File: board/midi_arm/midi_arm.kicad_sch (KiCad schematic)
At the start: 25 parts, among them J1 Conn_01x02_Pin, J2 Conn_01x02_Pin, J3 Conn_01x10_Pin, J4 RJ45, J5 Conn_01x03_Pin, J6 Conn_01x03_Pin, J7 Conn_01x03_Pin, U6 6DOF_6050

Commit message: BABOI 2.0 Board
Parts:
- removed C1, C2, C3: 100nF, Capacitor_SMD:C_01005_0402Metric, symbol Device:C
- removed J1, J2: Conn_01x02_Pin, Connector_PinHeader_2.54mm:PinHeader_1x02_P2.54mm_Vertical, symbol Connector:Conn_01x02_Pin
- removed J3: Conn_01x10_Pin, Connector_PinHeader_2.54mm:PinHeader_1x10_P2.54mm_Vertical, symbol Connector:Conn_01x10_Pin
- removed J4: RJ45, Connector_RJ:RJ45_Ninigi_GE, symbol Connector:RJ45
- removed J5, J6, J7: Conn_01x03_Pin, Connector_PinHeader_2.54mm:PinHeader_1x03_P2.54mm_Vertical, symbol Connector:Conn_01x03_Pin
- removed U1: ~, midi_arm:Wemos_S3_Mini_Outer_Pins, symbol midi_arm:Wemos_S3_Mini_Outer_Pins
- removed U2, U3, U4, U7: ~, midi_arm:TOUCH_BAR, symbol midi_arm:CAP_BUT_STRIP
- added H7, H8: MountingHole, MountingHole:MountingHole_2.2mm_M2, symbol Mechanical:MountingHole
- added J1: Conn_01x06_Pin, GPB_Footprints:JST_1x6_2.54, symbol Connector:Conn_01x06_Pin
- added J10, J5, J6, J7, J9: Conn_01x01_Pin, Connector_PinHeader_1.27mm:PinHeader_1x01_P1.27mm_Vertical, symbol Connector:Conn_01x01_Pin
- added J2: Conn_01x03_Pin, midi_arm:LED_conn, symbol Connector:Conn_01x03_Pin
- added J3: Conn_01x08_Pin, Connector_PinHeader_2.54mm:PinHeader_1x08_P2.54mm_Vertical, symbol Connector:Conn_01x08_Pin
- added J4: Conn_01x05_Pin, GPB_Footprints:JST_1x5_2.54_cablepad, symbol Connector:Conn_01x05_Pin
- added J8: Conn_01x06_Pin, GPB_Footprints:JST_1x6_2.54_cablepad, symbol Connector:Conn_01x06_Pin
- added R1, R11, R12, R13, R14, R16, R17, R18, R19, R2, R3, R4, R6, R7, R8, R9: 2.4k, Resistor_SMD:R_0805_2012Metric_Pad1.20x1.40mm_HandSolder, symbol Device:R
- added R10, R15, R20, R5: 24k, Resistor_SMD:R_0805_2012Metric_Pad1.20x1.40mm_HandSolder, symbol Device:R
- added RV1, RV2, RV3, RV4: R_Potentiometer_Small, midi_arm:pot_9.5x9.5, symbol Device:R_Potentiometer_Small
- added SW1, SW2, SW3, SW4: SW_MEC_5E, GPB_Footprints:switch_Touchpad, symbol Switch:SW_MEC_5E
- added U1: ~, GPB_Footprints:ESP32_S2_Wemos_Mini, symbol GPB_Parts:ESP32S2_Mini_Mod
- added U7, U9: ~, Package_DIP:DIP-8_W7.62mm, symbol midi_arm:MCP6002
- added U8: ~, midi_arm:ADS1115_mod, symbol midi_arm:ADS1115_mod
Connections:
- net GND1: now also J1.1 (Pin_1), J2.1 (Pin_1), J3.1 (Pin_1), SW1.3 (K), SW2.3 (K), SW3.3 (K), SW4.3 (K), U1.10A (GND), U1.10B (GND)
- net VBUS: now also J2.3 (Pin_3), J3.7 (Pin_7), U1.9A (VBUS)
- net at D2.2 (DOUT): now also J2.2 (Pin_2)
- net VCC_3V3: now reaches U5.1 (VCC)
- net VCC_3V3: now also J1.6 (Pin_6), J3.8 (Pin_8), U1.8A (VCC_3V3)
- net GLOVE_VCC: now reaches U6.1 (VCC)
- net GLOVE_VCC: now also J8.6 (Pin_6), R1.1, R11.1, R12.1, R16.1, R17.1, R3.1, R6.1, R7.1, U7.8 (VDD), U8.1 (Vcc), U9.8 (VDD)
- net GND2: now reaches U6.2 (GND)
- net GND2: now also J4.5 (Pin_5), J5.1 (Pin_1), J8.1 (Pin_1), R13.2, R18.2, R2.2, R8.2, U7.4 (GND), U8.2 (GND), U9.4 (GND)
- net GLOVE_SCL: now reaches U6.3 (SCL)
- net GLOVE_SCL: now also J8.3 (Pin_3), U8.3 (SCL)
- net GLOVE_SDA: now reaches U6.4 (SDA)
- net GLOVE_SDA: now also J8.4 (Pin_4), U8.4 (SDA)
- net GLOVE_ACC_INT: now reaches U6.8 (INT)
- net GLOVE_ACC_INT: now also J8.2 (Pin_2)
- net at D1.4 (DIN): now also U1.16A (GPIO_39)
- net SCL: now reaches U5.3 (SCL)
- net SCL: now also U1.3A (GPIO_5)
- net SDA: now reaches U5.4 (SDA)
- net SDA: now also U1.4A (GPIO_7)
- net at U5.8 (INT): now also U1.12A (GPIO_18)
- new net: SW1.2, U1.5A (GPIO_9)
- new net: R16.2, R18.1, R19.1
- new net: R19.2, R20.1, U9.6 (VinB-)
- new net: J10.1 (Pin_1), R17.2, RV1.2, U9.5 (VinB+)
- new net: R10.1, R9.2, U7.6 (VinB-)
- new net: R10.2, U7.7 (VoutB), U8.9 (A2)
- new net: J4.4 (Pin_4), RV4.1
- new net: J6.1 (Pin_1), R3.2, RV4.2, U7.3 (VinA+)
- new net: J4.1 (Pin_1), RV1.1
- new net: J4.2 (Pin_2), RV2.1
- new net: J4.3 (Pin_3), RV3.1
- new net: J7.1 (Pin_1), R7.2, RV3.2, U7.5 (VinB+)
- new net: R4.2, R5.1, U7.2 (VinA-)
- new net: R5.2, U7.1 (VoutA), U8.10 (A3)
- new net: R11.2, R13.1, R14.1
- new net: R14.2, R15.1, U9.2 (VinA-)
- new net: R20.2, U8.7 (A0), U9.7 (VoutB)
- new net: SW4.2, U1.2B (GPIO_2)
- new net: J9.1 (Pin_1), R12.2, RV2.2, U9.3 (VinA+)
- new net: R1.2, R2.1, R4.1
- new net: R6.2, R8.1, R9.1
- new net: SW2.2, U1.2A (GPIO_3)
- new net: SW3.2, U1.6B (GPIO_10)
- new net: R15.2, U8.8 (A1), U9.1 (VoutA)
- new net ALERT: J1.5 (Pin_5), U1.15A (GPIO_37)
- new net EXT_D0: J3.2 (Pin_2), U1.3B (GPIO_4)
- new net EXT_D1: J3.3 (Pin_3), U1.4B (GPIO_6)
- new net EXT_D2: J3.4 (Pin_4), U1.5B (GPIO_8)
- new net EXT_D3: J3.5 (Pin_5), U1.1B (GPIO_1)
- new net EXT_INT: J3.6 (Pin_6), U1.11A (GPIO_16)
- new net EXT_SCL: J1.3 (Pin_3), U1.12B (GPIO_21)
- new net EXT_SDA: J1.4 (Pin_4), U1.16B (GPIO_40)
- new net GLOVE_ADC_ALERT: J8.5 (Pin_5), U8.6 (ALERT)
- new net INT: J1.2 (Pin_2), U1.14A (GPIO_35)
- no-connect marks 11 -> 32
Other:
- note added: "A"
- note added: "B"
- note added: "C"
- note added: "CTRL"
- note added: "Design Target for Tension Strips is 1.4 - 1.6 kOhm +/- 500 Ohm"
- note added: "ESP32-S2"
- note added: "Extension Port"
- note added: "Glove Board"
- note added: "Glove Board Conn"
- note added: "Glove Connector"
- note added: "LED"
- note added: "Tension Strips"
- note removed: "3_3V"
- note removed: "TOUCH1"
- note removed: "TOUCH2"
- note removed: "TOUCH3"
- note removed: "VBUS"
- title: (none) -> BABOI
- moved on the sheet: D1, D2, H1, H2, H3, H4, H5, H6, U5, U6

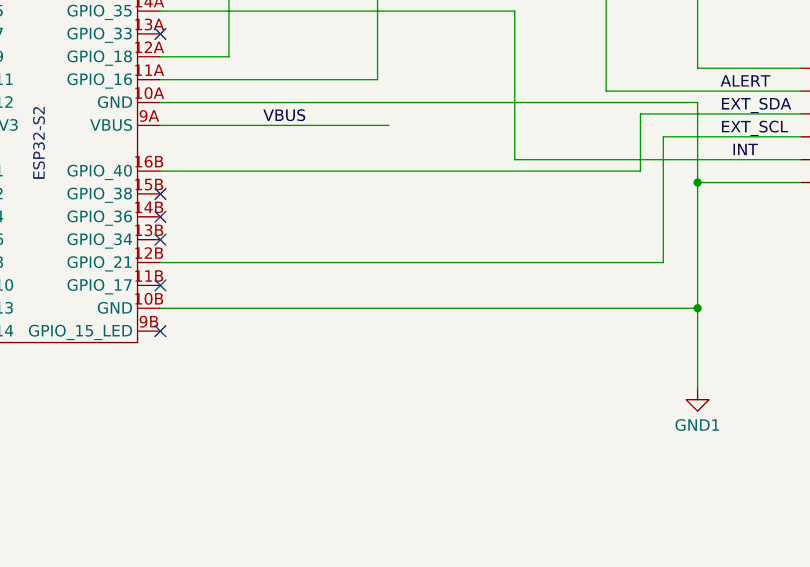
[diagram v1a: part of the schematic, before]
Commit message: Add support for touchpads vs buttons
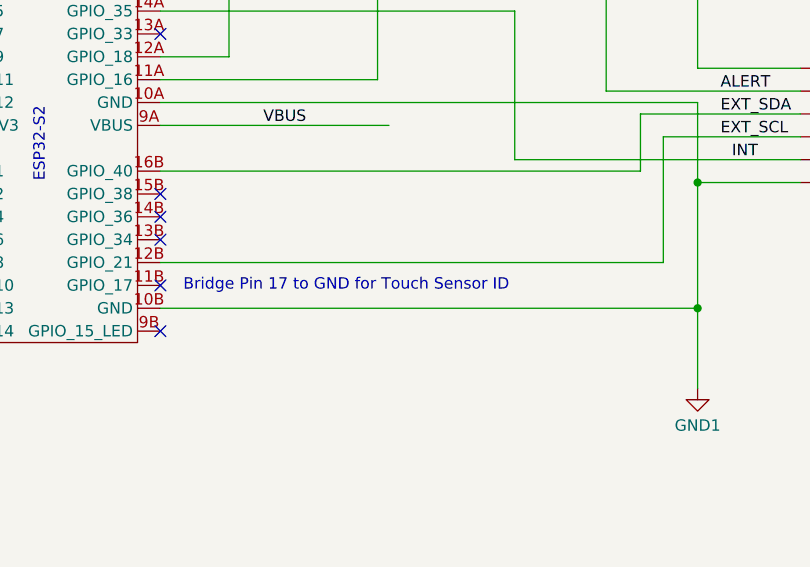
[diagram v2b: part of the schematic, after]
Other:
- note added: "Bridge Pin 17 to GND for Touch Sensor ID"
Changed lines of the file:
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@@
+    (effects (font (size 1.27 1.27)) (justify left bottom))
+  )
+  (text "Bridge Pin 17 to GND for Touch Sensor ID" (at 194.31 129.032 0)
     (effects (font (size 1.27 1.27)) (justify left bottom))
   )

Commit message: updates
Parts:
- R12, R17, R3, R7: value 2.4k -> 5.1k
- R13, R14, R18, R19, R2, R4, R8, R9: value 2.4k -> 3.3k
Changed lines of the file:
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@@
       (effects (font (size 1.27 1.27)))
     )
-    (property "Value" "2.4k" (at 77.47 29.0139 90)
+    (property "Value" "3.3k" (at 77.47 29.0139 90)
       (effects (font (size 1.27 1.27)))
     )
@@
       (effects (font (size 1.27 1.27)))
     )
-    (property "Value" "2.4k" (at 34.29 34.0939 90)
+    (property "Value" "5.1k" (at 34.29 34.0939 90)
       (effects (font (size 1.27 1.27)))
     )
@@
       (effects (font (size 1.27 1.27)))
     )
-    (property "Value" "2.4k" (at 77.47 46.7939 90)
+    (property "Value" "3.3k" (at 77.47 46.7939 90)
       (effects (font (size 1.27 1.27)))
     )
@@
       (effects (font (size 1.27 1.27)))
     )
-    (property "Value" "2.4k" (at 77.47 82.3539 90)
+    (property "Value" "3.3k" (at 77.47 82.3539 90)
       (effects (font (size 1.27 1.27)))
     )
@@
       (effects (font (size 1.27 1.27)))
     )
-    (property "Value" "2.4k" (at 34.29 87.4339 90)
+    (property "Value" "5.1k" (at 34.29 87.4339 90)
       (effects (font (size 1.27 1.27)))
     )
@@
       (effects (font (size 1.27 1.27)))
     )
-    (property "Value" "2.4k" (at 34.29 51.8739 90)
+    (property "Value" "5.1k" (at 34.29 51.8739 90)
       (effects (font (size 1.27 1.27)))
     )
@@
       (effects (font (size 1.27 1.27)))
     )
-    (property "Value" "2.4k" (at 77.47 64.5739 90)
+    (property "Value" "3.3k" (at 77.47 64.5739 90)
       (effects (font (size 1.27 1.27)))
     )
@@
       (effects (font (size 1.27 1.27)))
     )
-    (property "Value" "2.4k" (at 34.29 69.6539 90)
+    (property "Value" "5.1k" (at 34.29 69.6539 90)
       (effects (font (size 1.27 1.27)))
     )
@@
       (effects (font (size 1.27 1.27)))
     )
-    (property "Value" "2.4k" (at 46.99 25.2039 90)
+    (property "Value" "3.3k" (at 46.99 25.2039 90)
       (effects (font (size 1.27 1.27)))
     )
@@
       (effects (font (size 1.27 1.27)))
     )
-    (property "Value" "2.4k" (at 46.99 60.7639 90)
+    (property "Value" "3.3k" (at 46.99 60.7639 90)
       (effects (font (size 1.27 1.27)))
     )
@@
       (effects (font (size 1.27 1.27)))
     )
-    (property "Value" "2.4k" (at 46.99 78.5439 90)
+    (property "Value" "3.3k" (at 46.99 78.5439 90)
       (effects (font (size 1.27 1.27)))
     )
@@
       (effects (font (size 1.27 1.27)))
     )
-    (property "Value" "2.4k" (at 46.99 42.9839 90)
-      (effects (font (size 1.27 1.27)))
-    )
+    (property "Value" "3.3k" (at 46.99 42.9839 90)
+      (effects (font (size 1.27 1.27)))
+    )

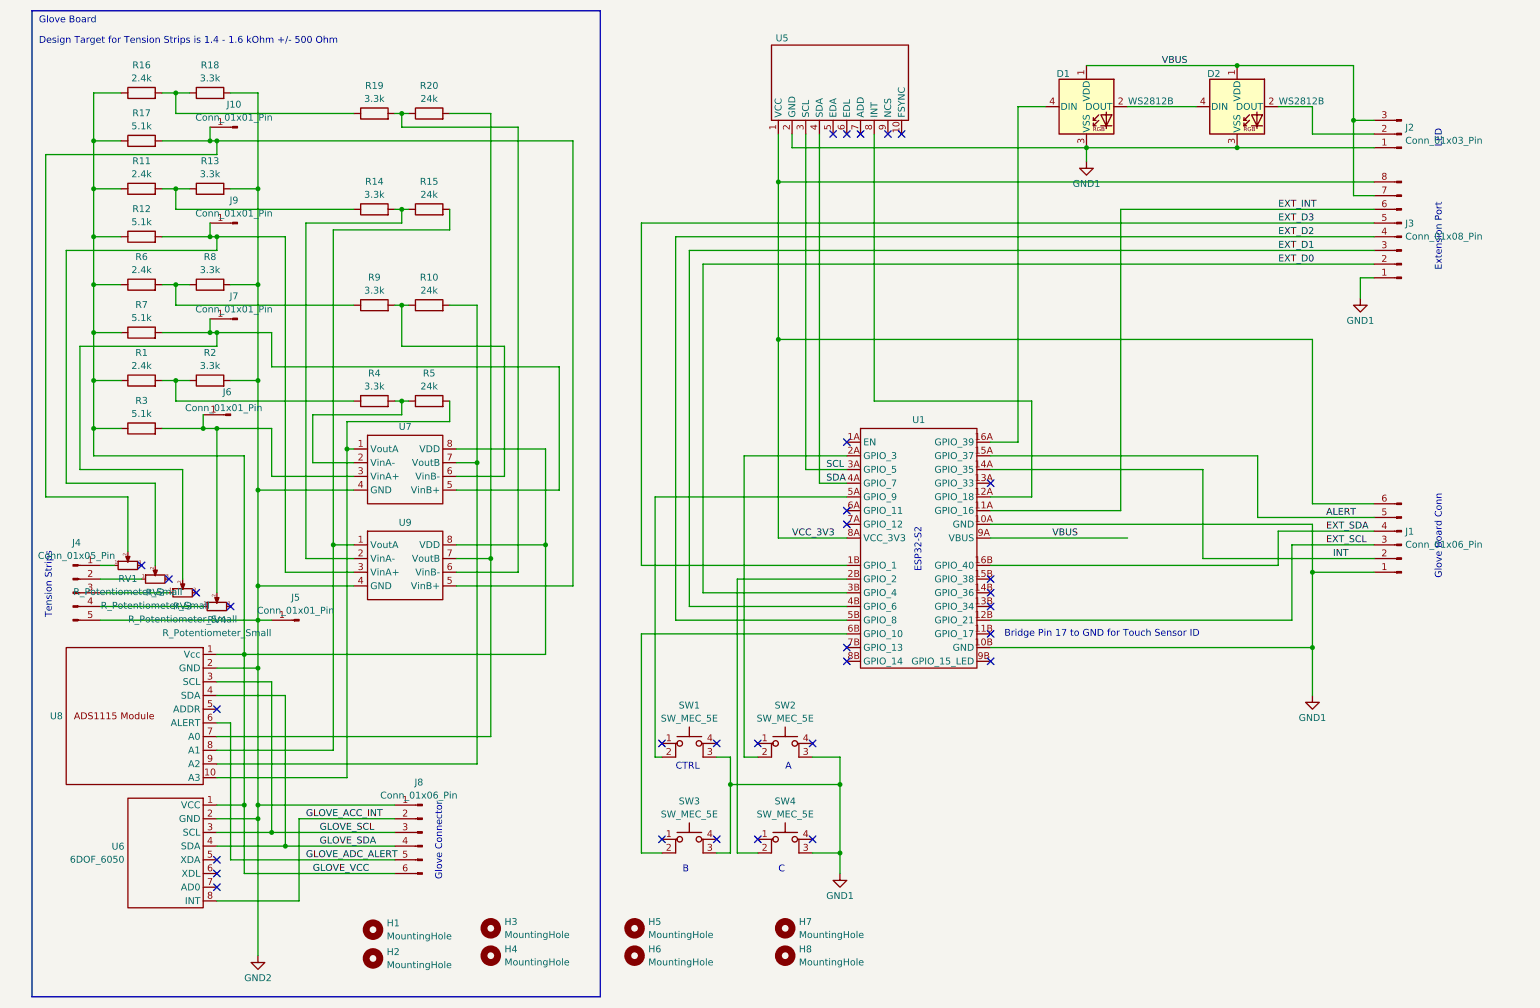
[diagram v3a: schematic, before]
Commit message: HW Version 3 Support
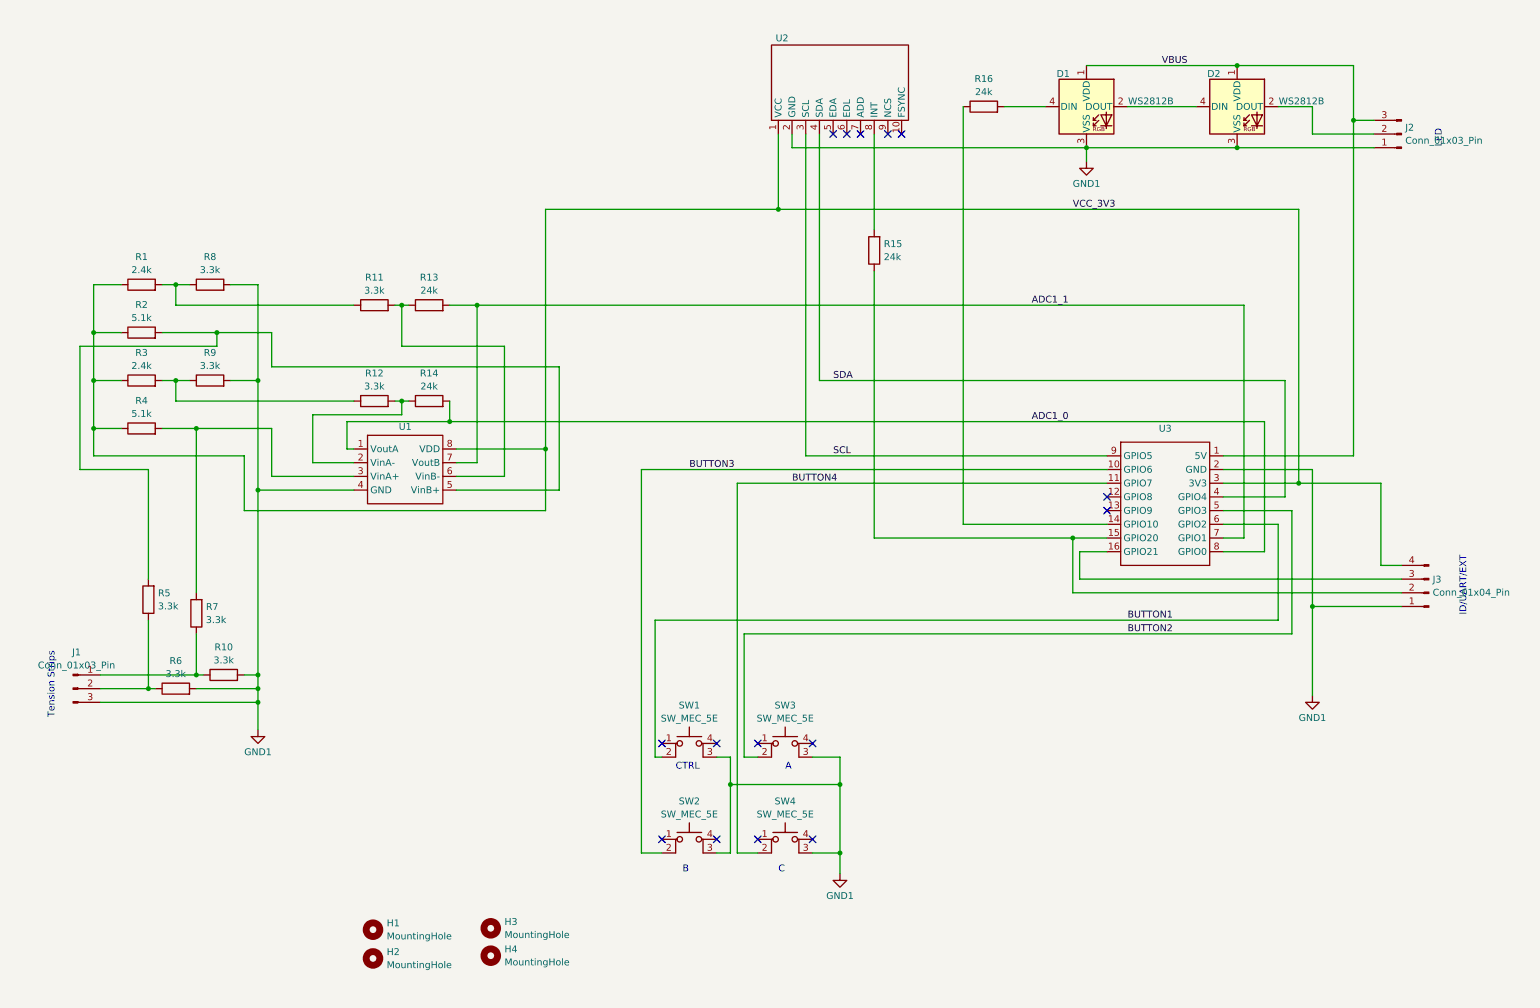
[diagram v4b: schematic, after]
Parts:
- removed H5, H6, H7, H8: MountingHole, MountingHole:MountingHole_2.2mm_M2, symbol Mechanical:MountingHole
- removed J1: Conn_01x06_Pin, GPB_Footprints:JST_1x6_2.54, symbol Connector:Conn_01x06_Pin
- removed J10, J5, J6, J7, J9: Conn_01x01_Pin, Connector_PinHeader_1.27mm:PinHeader_1x01_P1.27mm_Vertical, symbol Connector:Conn_01x01_Pin
- removed J3: Conn_01x08_Pin, Connector_PinHeader_2.54mm:PinHeader_1x08_P2.54mm_Vertical, symbol Connector:Conn_01x08_Pin
- removed J4: Conn_01x05_Pin, GPB_Footprints:JST_1x5_2.54_cablepad, symbol Connector:Conn_01x05_Pin
- removed J8: Conn_01x06_Pin, GPB_Footprints:JST_1x6_2.54_cablepad, symbol Connector:Conn_01x06_Pin
- removed R11: 2.4k, Resistor_SMD:R_0805_2012Metric_Pad1.20x1.40mm_HandSolder, symbol Device:R
- removed R12, R17: 5.1k, Resistor_SMD:R_0805_2012Metric_Pad1.20x1.40mm_HandSolder, symbol Device:R
- removed R13, R14, R18, R19: 3.3k, Resistor_SMD:R_0805_2012Metric_Pad1.20x1.40mm_HandSolder, symbol Device:R
- removed R20: 24k, Resistor_SMD:R_0805_2012Metric_Pad1.20x1.40mm_HandSolder, symbol Device:R
- removed RV1, RV2, RV3, RV4: R_Potentiometer_Small, midi_arm:pot_9.5x9.5, symbol Device:R_Potentiometer_Small
- removed U1: ~, GPB_Footprints:ESP32_S2_Wemos_Mini, symbol GPB_Parts:ESP32S2_Mini_Mod
- removed U6: 6DOF_6050, midi_arm:6050_MOD, symbol midi_arm:6DOF_6050
- removed U8: ~, midi_arm:ADS1115_mod, symbol midi_arm:ADS1115_mod
- removed U9: ~, Package_DIP:DIP-8_W7.62mm, symbol midi_arm:MCP6002
- added J1: Conn_01x03_Pin, midi_arm:LED_conn, symbol Connector:Conn_01x03_Pin
- added J3: Conn_01x04_Pin, Connector_PinHeader_2.54mm:PinHeader_1x04_P2.54mm_Vertical, symbol Connector:Conn_01x04_Pin
- added R10, R5, R6, R7: 3.3k, Resistor_SMD:R_0805_2012Metric_Pad1.20x1.40mm_HandSolder, symbol Device:R
- added U3: ~, midi_arm:ESP32-C3_SuperMini, symbol midi_arm:ESP32-C3_SuperMini
- R16: value 2.4k -> 24k
- SW1, SW4: footprint GPB_Footprints:switch_Touchpad -> GPB_Footprints:switch_Simple
- SW2: renamed from SW3; footprint GPB_Footprints:switch_Touchpad -> GPB_Footprints:switch_Simple
- SW3: renamed from SW2; footprint GPB_Footprints:switch_Touchpad -> GPB_Footprints:switch_Simple
- renumbered R6 to R1, R9 to R11, R4 to R12, R10 to R13, R5 to R14, R7 to R2, R1 to R3, R3 to R4, R2 to R9, U7 to U1, U5 to U2
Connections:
- net GND2 is gone; now on net GND1: R8.2, R9.2, U1.4 (GND)
- net GND1: now also J1.3 (Pin_3), J3.1 (Pin_1), R10.2, R6.2, U3.2 (GND)
- net SCL: now also U3.9 (GPIO5)
- net SDA: now also U3.4 (GPIO4)
- net VBUS: now also U3.1 (5V)
- net VCC_3V3: now also R1.1, R2.1, R3.1, R4.1, U1.8 (VDD), J3.4 (Pin_4), U3.3 (3V3)
- net BUTTON1: now reaches SW1.2
- net BUTTON1: now also U3.6 (GPIO2)
- net at R16.2: now also D1.4 (DIN)
- net ADC1_1: now reaches R13.2, U1.7 (VoutB)
- net ADC1_1: now also U3.7 (GPIO1)
- net at R4.2, U1.3 (VinA+): now also R7.2
- net at R2.2, U1.5 (VinB+): now also R5.2
- net ADC1_0: now reaches R14.2, U1.1 (VoutA)
- net ADC1_0: now also U3.8 (GPIO0)
- net at R15.1: now also J3.2 (Pin_2), U3.15 (GPIO20)
- net BUTTON4: now reaches SW4.2
- net BUTTON4: now also U3.11 (GPIO7)
- net at U2.8 (INT): now also R15.2
- net BUTTON2: now reaches SW3.2
- net BUTTON2: now also U3.5 (GPIO3)
- net BUTTON3: now reaches SW2.2
- net BUTTON3: now also U3.10 (GPIO6)
- removed net GLOVE_VCC: R1.1, R16.1, R2.1, R3.1, R4.1, U1.8 (VDD)
- new net: J1.2 (Pin_2), R5.1, R6.1
- new net: J1.1 (Pin_1), R10.1, R7.1
- new net: J3.3 (Pin_3), U3.16 (GPIO21)
- new net: R16.1, U3.14 (GPIO10)
- no-connect marks 32 -> 15
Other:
- note added: "ID/UART/EXT"
- note removed: "Bridge Pin 17 to GND for Touch Sensor ID"
- note removed: "Design Target for Tension Strips is 1.4 - 1.6 kOhm +/- 500 Ohm"
- note removed: "ESP32-S2"
- note removed: "Extension Port"
- note removed: "Glove Board"
- note removed: "Glove Board Conn"
- note removed: "Glove Connector"
